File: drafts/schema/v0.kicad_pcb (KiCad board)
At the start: 2 copper layers, 36 parts, among them P1 CONN_BATT/SW, P2 CONN_SW/MOT, P3 CONN_SERIAL, Q1 P/N_MOS, Q2 P/N_MOS, U1 WeMos_mini, U2 N9505, U3 VHN5180A-E

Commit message: begun a PCB draft
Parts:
- C2, C3, Q2, R10, R11, R12, R7, R8, R9, U2: moved to B.Cu
- P1: value CONN_BATT/SW -> CONN_BATT/MOT
- P2: value CONN_SW/MOT -> CONN_SW
- R13: footprint Resistors_SMD:R_0805_HandSoldering -> Resistors_SMD:R_1206_HandSoldering; moved to B.Cu
- R14: footprint Resistors_SMD:R_0805_HandSoldering -> Resistors_SMD:R_1206_HandSoldering
- moved R7 100.8 mm to (173.4, 56.5), turned to 90 degrees
- moved Q2 89.5 mm to (168.7, 66.9), turned to 90 degrees
- moved P1 87.1 mm to (133.2, 52.6)
- moved R8 86.4 mm to (171.1, 56.5), turned to 90 degrees
- moved C3 74.8 mm to (125.5, 49.4)
- moved D1 73.9 mm to (140.8, 69.7)
- moved R10 73.9 mm to (170.1, 63.2), turned to 180 degrees
- moved R17 66.1 mm to (126.7, 58.9)
- moved P3 65.3 mm to (153.5, 60.3), turned to 270 degrees
- moved C2 64.5 mm to (124.3, 67.8), turned to 90 degrees
- moved D3 61.0 mm to (152.2, 84.3), turned to 90 degrees
- moved R18 58.2 mm to (137.9, 73.6)
- moved R14 57.5 mm to (131.9, 73.4), turned to 180 degrees
- moved P2 56.2 mm to (112.8, 60.2), turned to 90 degrees
- moved R6 51.5 mm to (124.3, 67.8), turned to 90 degrees
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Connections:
- P2 pad 5: (no net) -> /TX
- P3 pad 1: /SER_3V3 -> /SCL
- P3 pad 2: GND -> /SDA
- P3 pad 4: /SDA -> GND
- P3 pad 5: /SCL -> /SER_3V3
- U1 pad 8: (no net) -> /TX
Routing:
- net GND: track 0.00 -> 158.9 mm, vias 0 -> 4
- net /BATT+: track 0.00 -> 101.2 mm
- net VCC: track 0.00 -> 52.5 mm
- net /TX: track 0.00 -> 49.7 mm
- net /SWITCH_A: track 0.00 -> 36.8 mm, vias 0 -> 2
- net /MOT_B: track 0.00 -> 33.2 mm
- net /SW_A: track 0.00 -> 31.9 mm, vias 0 -> 2
- net /MOT_A: track 0.00 -> 28.0 mm
- net Net-(R15-Pad1): track 0.00 -> 27.5 mm, vias 0 -> 2
- net /SCL: track 0.00 -> 26.4 mm
- net /SW_B: track 0.00 -> 25.4 mm
- net /SDA: track 0.00 -> 23.9 mm
- net /EN_DIAG_B: track 0.00 -> 23.2 mm, vias 0 -> 3
- net /OW: track 0.00 -> 21.4 mm
- net Net-(Q1-Pad4): track 0.00 -> 11.7 mm
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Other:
- net class Default: clearance 0.2 -> 0.015
- rule trace_clearance: 0.2 -> 0.015

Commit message: routed first draft
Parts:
- added J1: CONN_01X01, Mounting_Holes:MountingHole_3.2mm_M3, F.Cu at (114.1, 90.0)
- added J2: CONN_01X01, Mounting_Holes:MountingHole_3.2mm_M3, F.Cu at (152.9, 90.0)
- added J3: CONN_01X01, Mounting_Holes:MountingHole_3.2mm_M3, F.Cu at (152.2, 52.6)
- added J4: CONN_01X01, Mounting_Holes:MountingHole_3.2mm_M3, F.Cu at (114.1, 52.6)
- Q1, R1, R2, R20, R21, R3, R4, R5: moved to B.Cu
- R13: footprint Resistors_SMD:R_1206_HandSoldering -> Resistors_SMD:R_0805_HandSoldering; moved to F.Cu
- R14: footprint Resistors_SMD:R_1206_HandSoldering -> Resistors_SMD:R_0805_HandSoldering
- U1: footprint wemos_d1_mini:D1_mini_board -> wemos_d1_mini:Wemos-D1-mini
- moved R7 45.7 mm to (132.0, 75.8)
- moved R8 45.7 mm to (129.7, 75.8)
- moved R11 44.9 mm to (129.9, 85.1), turned to 0 degrees
- moved R9 44.8 mm to (127.4, 75.8)
- moved R12 44.2 mm to (133.5, 81.7), turned to 90 degrees
- moved R10 43.7 mm to (129.8, 80.3)
- moved Q2 41.9 mm to (129.8, 82.7), turned to 0 degrees
- moved C4 21.9 mm to (133.8, 90.9), turned to 0 degrees
- moved D3 18.8 mm to (133.8, 88.3), turned to 0 degrees
- moved U2 15.0 mm to (133.2, 70.4), turned to 270 degrees
- moved D2 13.3 mm to (125.0, 84.5), turned to 90 degrees
- moved R1 11.0 mm to (141.1, 76.1), turned to 90 degrees
- moved P2 10.1 mm to (112.8, 70.3), turned to 270 degrees
- moved P3 10.1 mm to (153.5, 70.4), turned to 90 degrees
- moved R2 7.83 mm to (138.8, 76.1), turned to 90 degrees
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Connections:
- P1 pad 1: /BATT+ -> /MOT_B
- P1 pad 2: GND -> /MOT_A
- P1 pad 4: /MOT_A -> GND
- P1 pad 5: /MOT_B -> /BATT+
- P2 pad 1: /SW_V+ -> /TX
- P2 pad 2: GND -> /SWITCH_B
- P2 pad 4: /SWITCH_B -> GND
- P2 pad 5: /TX -> /SW_V+
- P3 pad 1: /SCL -> /SER_3V3
- P3 pad 2: /SDA -> GND
- P3 pad 4: GND -> /SDA
- P3 pad 5: /SER_3V3 -> /SCL
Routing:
- net GND: track 158.9 -> 254.5 mm, vias 4 -> 3
- net /BATT+: track 101.2 -> 53.6 mm, vias 0 -> 1
- net /3V3: track 4.57 -> 30.0 mm
- net /EN_DRIVER: track 10.5 -> 30.3 mm, vias 0 -> 3
- net /SW_V+: track 0.00 -> 16.7 mm
- net /SER_3V3: track 0.00 -> 16.4 mm
- net /SWITCH_B: track 0.00 -> 11.7 mm
- net /SCL: track 26.4 -> 16.3 mm
- net VCC: track 52.5 -> 62.5 mm
- net /SDA: track 23.9 -> 14.6 mm
- net /OW: track 21.4 -> 12.2 mm
- net /SW_B: track 25.4 -> 33.6 mm, vias 0 -> 1
- net /TX: track 49.7 -> 55.9 mm
- net Net-(Q2-Pad6): track 7.81 -> 2.48 mm
- net Net-(R15-Pad1): track 27.5 -> 23.5 mm
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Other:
- board outline added: 52.1 x 52.3 mm
- net class Default: clearance 0.015 -> 0.14
- rule trace_clearance: 0.015 -> 0.14

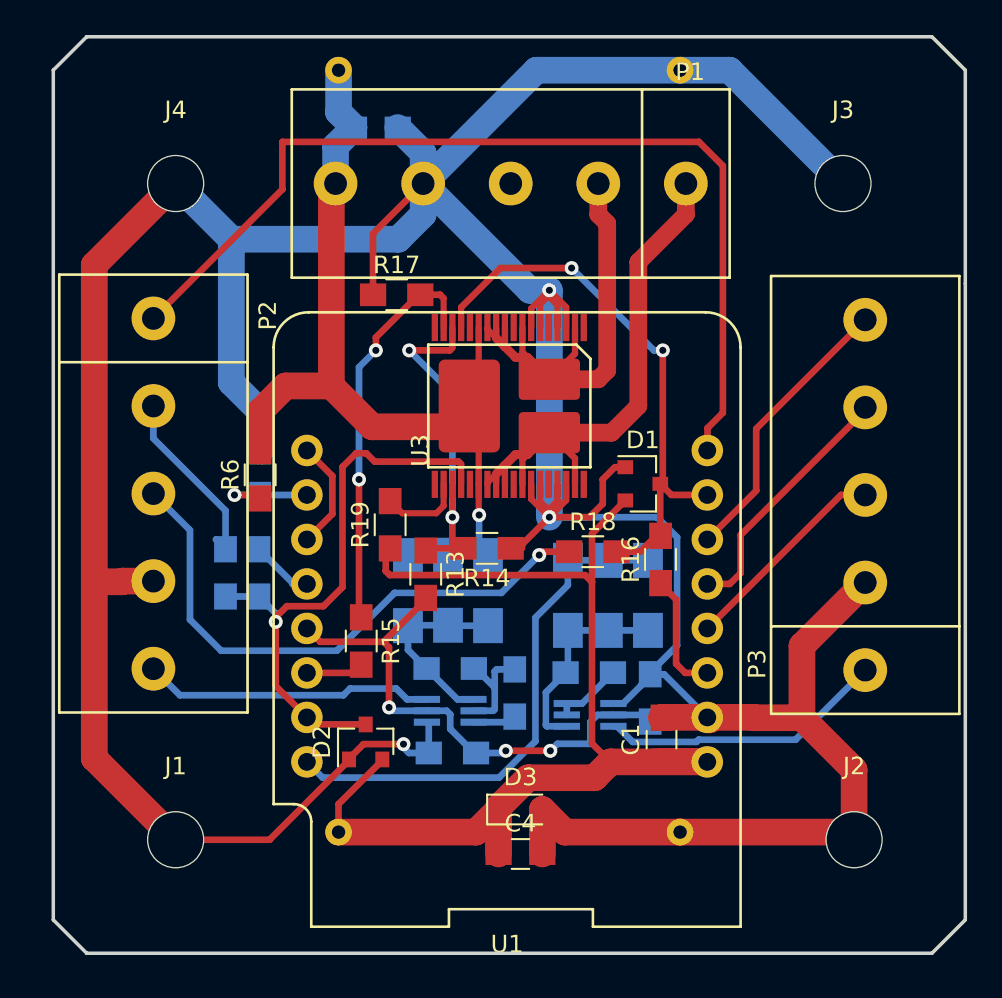
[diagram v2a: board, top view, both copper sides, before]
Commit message: refactored library/shapes/footprint files placement
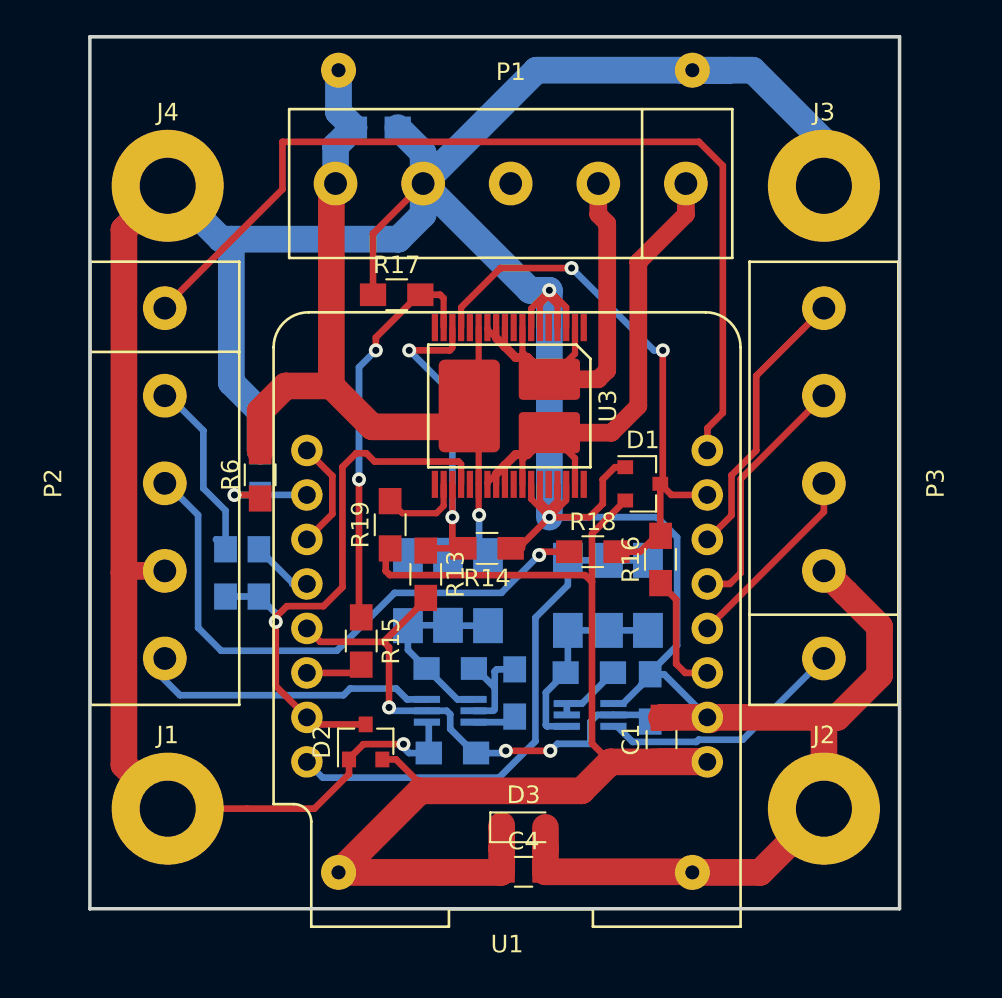
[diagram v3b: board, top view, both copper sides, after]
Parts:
- J1, J2, J3, J4: footprint Mounting_Holes:MountingHole_3.2mm_M3 -> Mounting_Holes:MountingHole_3.2mm_M3_Pad
- U1: footprint wemos_d1_mini:Wemos-D1-mini -> wemos-d1-mini:wemos-d1-mini
- U2: footprint n9505-step-down-footprint:step-down-n9505 -> n9505-step-down:n9595
- U3: footprint PowerSSO-36-TP:PowerSOIC-36 -> power-sso-36-tp:PowerSOIC-36
- moved J2 2.47 mm to (151.1, 88.3)
- moved P3 2.45 mm to (151.1, 69.7)
- moved J1 1.83 mm to (113.7, 88.3)
- moved U2 1.39 mm to (133.5, 69.0)
- moved J3 1.10 mm to (151.1, 52.7)
- moved C4 1.03 mm to (134.0, 91.9)
- moved D3 1.03 mm to (134.0, 89.3)
- moved P2 0.88 mm to (113.5, 69.7)
- moved J4 0.47 mm to (113.7, 52.7)
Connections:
- P1 pad 3: (no net) -> Net-(P1-Pad3)
- U3 pad 1: (no net) -> Net-(U3-Pad1)
- U3 pad 14: (no net) -> Net-(U3-Pad14)
- U3 pad 18: (no net) -> Net-(U3-Pad18)
- U3 pad 19: (no net) -> Net-(U3-Pad19)
- U3 pad 23: (no net) -> Net-(U3-Pad23)
- U3 pad 28: (no net) -> Net-(U3-Pad28)
- U3 pad 32: (no net) -> Net-(U3-Pad32)
- U3 pad 36: (no net) -> Net-(U3-Pad36)
- U3 pad 5: (no net) -> Net-(U3-Pad5)
- U3 pad 9: (no net) -> Net-(U3-Pad9)
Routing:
- net VCC: track 62.5 -> 70.8 mm
- net GND: track 254.5 -> 252.4 mm
- net /SER_3V3: track 16.4 -> 14.4 mm
- net /OW: track 12.2 -> 11.0 mm
- net /SWITCH_B: track 11.7 -> 11.1 mm
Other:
- board size 52.1 x 52.3 mm -> 46.2 x 49.8 mm
